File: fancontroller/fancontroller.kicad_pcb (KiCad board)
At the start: 2 copper layers, 84 x 80 mm, 43 parts, among them J1 Power, J2 Serial Conn, M1 FAN0, M2 FAN0, M3 FAN0, M4 FAN0, M5 FAN0, M6 FAN0, Q1 AO3400A, Q10 AO3401A, Q11 AO3400A, Q12 AO3401A, Q2 AO3401A, Q3 AO3400A, Q4 AO3401A, Q5 AO3400A, Q6 AO3401A, Q7 AO3400A, Q8 AO3401A, Q9 AO3400A, SW1 SW_Push, U2 ESP32-WROOM-32, U3 AMS1117-3.3

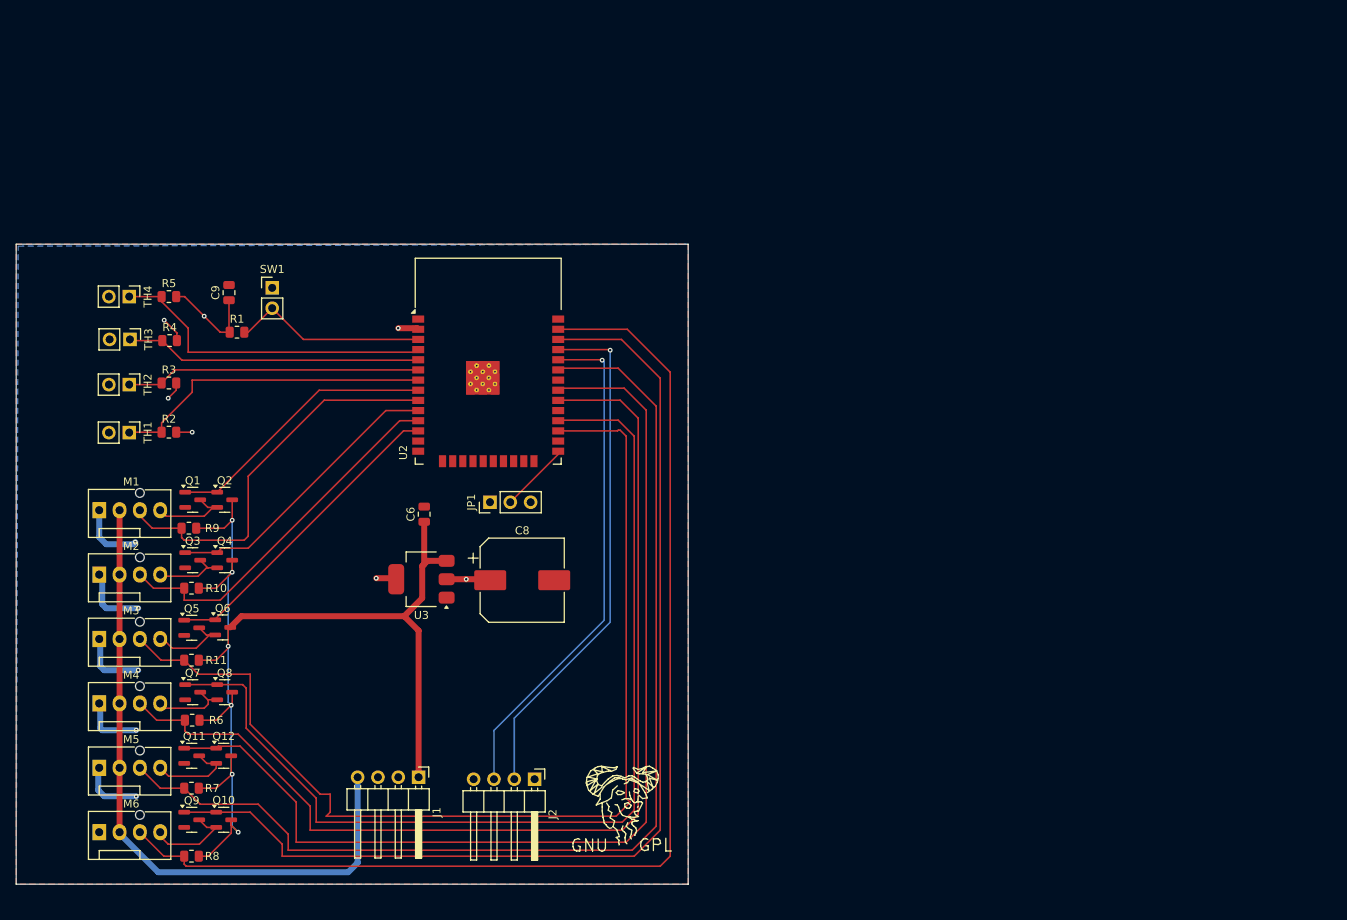
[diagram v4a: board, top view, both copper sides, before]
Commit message: Improve footprints and do massive overhaul for part numbering for better future order
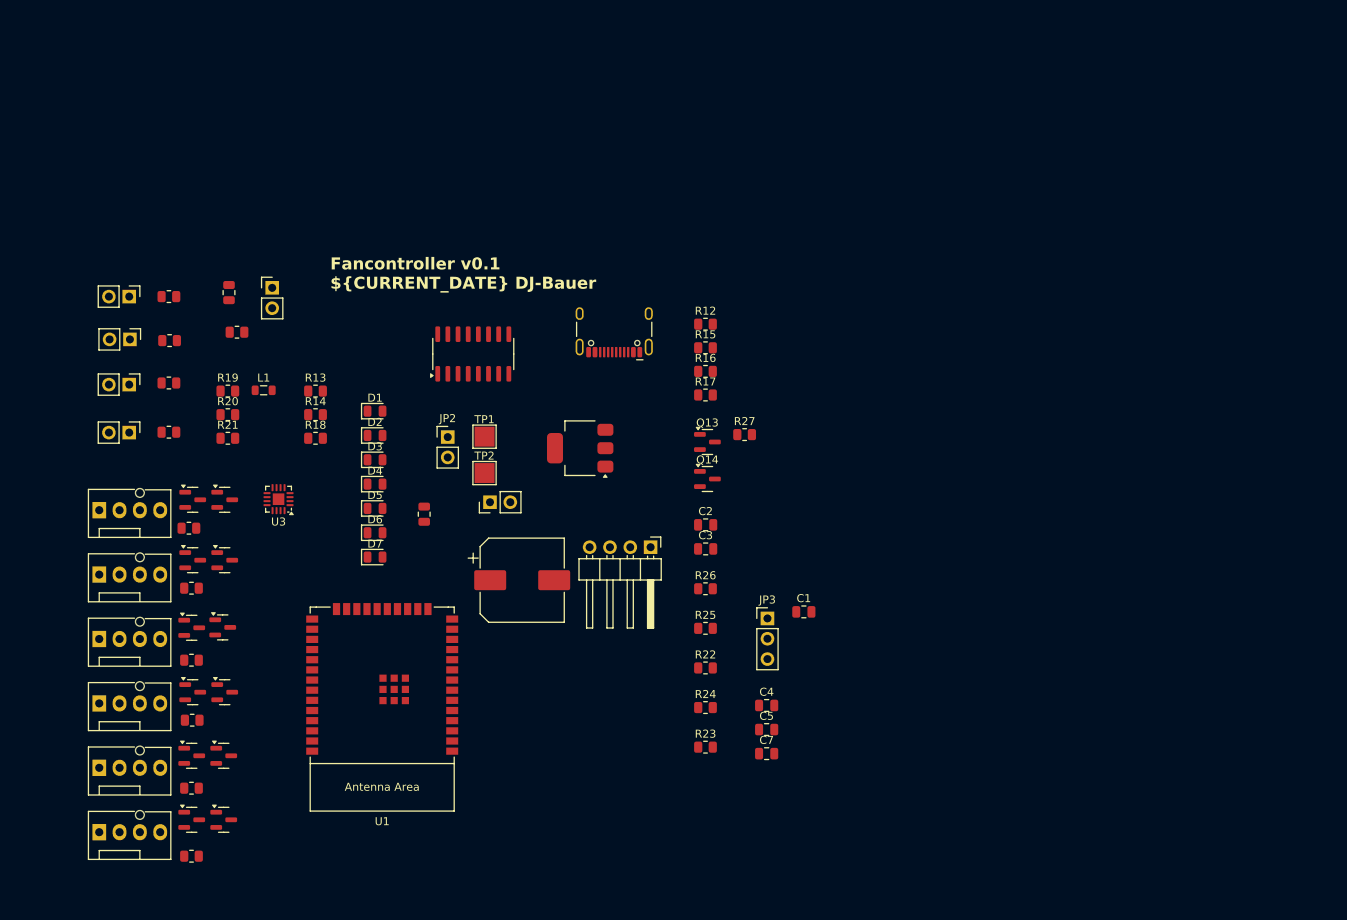
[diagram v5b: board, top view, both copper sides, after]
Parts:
- removed J2: Serial Conn, Connector_PinHeader_2.54mm:PinHeader_1x04_P2.54mm_Horizontal
- removed REF**: Symbol_GNU-Logo_SilkscreenTop, Symbol:Symbol_GNU-Logo_SilkscreenTop
- added C1: 100nF, Capacitor_SMD:C_0805_2012Metric, F.Cu at (122.0, 134.5)
- added C2: 100nF, Capacitor_SMD:C_0805_2012Metric, F.Cu at (109.7, 123.6)
- added C3: 100nF, Capacitor_SMD:C_0805_2012Metric, F.Cu at (109.7, 126.6)
- added C4: 10uF, Capacitor_SMD:C_0805_2012Metric, F.Cu at (117.3, 146.2)
- added C5: 100nF, Capacitor_SMD:C_0805_2012Metric, F.Cu at (117.3, 149.2)
- added C7: 10uF, Capacitor_SMD:C_0805_2012Metric, F.Cu at (117.3, 152.2)
- added D1: EN, LED_SMD:LED_0805_2012Metric, F.Cu at (68.4, 109.4)
- added D2: 3.3V, LED_SMD:LED_0805_2012Metric, F.Cu at (68.4, 112.4)
- added D3: 5V, LED_SMD:LED_0805_2012Metric, F.Cu at (68.4, 115.5)
- added D4: 12V, LED_SMD:LED_0805_2012Metric, F.Cu at (68.4, 118.5)
- added D5: TX, LED_SMD:LED_0805_2012Metric, F.Cu at (68.4, 121.5)
- added D6: RX, LED_SMD:LED_0805_2012Metric, F.Cu at (68.4, 124.6)
- added D7: Reset, LED_SMD:LED_0805_2012Metric, F.Cu at (68.4, 127.6)
- added JP2: PDG is ground, Connector_PinHeader_2.54mm:PinHeader_1x02_P2.54mm_Vertical, F.Cu at (77.4, 112.6)
- added JP3: BOOT, Connector_PinHeader_2.54mm:PinHeader_1x03_P2.54mm_Vertical, F.Cu at (117.4, 135.3)
- added L1: 2.2uH, Inductor_SMD:L_0805_2012Metric, F.Cu at (54.4, 106.8)
- added P2: USB_C_Plug_USB2.0, Connector_USB:USB_C_Receptacle_HCTL_HC-TYPE-C-16P-01A, F.Cu at (98.2, 98.2)
- added Q13: AO3400A, Package_TO_SOT_SMD:SOT-23, F.Cu at (109.9, 113.2)
- added Q14: AO3401A, Package_TO_SOT_SMD:SOT-23, F.Cu at (109.9, 117.8)
- added R12: 60, Resistor_SMD:R_0805_2012Metric, F.Cu at (109.7, 98.5)
- added R13: 65, Resistor_SMD:R_0805_2012Metric, F.Cu at (60.9, 106.9)
- added R14: 150, Resistor_SMD:R_0805_2012Metric, F.Cu at (60.9, 109.8)
- added R15: 1k, Resistor_SMD:R_0805_2012Metric, F.Cu at (109.7, 101.5)
- added R16: 60, Resistor_SMD:R_0805_2012Metric, F.Cu at (109.7, 104.4)
- added R17: 60, Resistor_SMD:R_0805_2012Metric, F.Cu at (109.7, 107.3)
- added R18: 65, Resistor_SMD:R_0805_2012Metric, F.Cu at (60.9, 112.8)
- added R19: 100k, Resistor_SMD:R_0805_2012Metric, F.Cu at (50.0, 106.9)
- added R20: 270k, Resistor_SMD:R_0805_2012Metric, F.Cu at (50.0, 109.8)
- added R21: 51k, Resistor_SMD:R_0805_2012Metric, F.Cu at (50.0, 112.8)
- added R22: 10k, Resistor_SMD:R_0805_2012Metric, F.Cu at (109.7, 141.5)
- added R23: 10k, Resistor_SMD:R_0805_2012Metric, F.Cu at (109.7, 151.4)
- added R24: 10k, Resistor_SMD:R_0805_2012Metric, F.Cu at (109.7, 146.4)
- added R25: 10k, Resistor_SMD:R_0805_2012Metric, F.Cu at (109.7, 136.5)
- added R26: 10k, Resistor_SMD:R_0805_2012Metric, F.Cu at (109.7, 131.6)
- added R27: 10k, Resistor_SMD:R_0805_2012Metric, F.Cu at (114.6, 112.3)
- added TP1: V_out, TestPoint:TestPoint_Pad_2.5x2.5mm, F.Cu at (82.0, 112.6)
- added TP2: PGD, TestPoint:TestPoint_Pad_2.5x2.5mm, F.Cu at (82.0, 117.1)
- added U1: ESP32-WROOM-32, PCM_Espressif:ESP32-WROOM-32E, F.Cu at (69.2, 144.9)
- added U4: AMS1117-3.3, Package_TO_SOT_SMD:SOT-223-3_TabPin2, F.Cu at (94.0, 114.0)
- C6: value 10uF -> 47u
- C9: value 0.1uF -> 100nF
- JP1: value BOOT -> Enable 12V Power; footprint Connector_PinHeader_2.54mm:PinHeader_1x03_P2.54mm_Vertical -> Connector_PinHeader_2.54mm:PinHeader_1x02_P2.54mm_Vertical
- Q1: value AO3400A -> SS8050-G
- Q2: value AO3401A -> SS8050-G
- R10, R11: value 10k -> 470
- R6, R7: value 10k -> 5.1k
- SW1: value SW_Push -> Reset
- TH1: value Thermistor -> Temp0
- TH2: value Thermistor -> Temp1
- TH3: value Thermistor -> Temp2
- TH4: value Thermistor -> Temp3
- U2: value ESP32-WROOM-32 -> CH340C; footprint RF_Module:ESP32-WROOM-32 -> Package_SO:SOIC-16_3.9x9.9mm_P1.27mm
- U3: value AMS1117-3.3 -> BD9D300MUV; footprint Package_TO_SOT_SMD:SOT-223-3_TabPin2 -> Package_DFN_QFN:VQFN-16-1EP_3x3mm_P0.5mm_EP1.45x1.45mm
- moved J1 40.8 mm to (102.8, 126.4)
- moved U3 20.5 mm to (56.3, 120.4)
- moved U2 4.31 mm to (80.6, 102.2), turned to 90 degrees
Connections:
- JP1 pad 1: +3.3V -> +12V
- JP1 pad 2: Net-(JP1-C) -> /Power Delivery/EN
- M1 pad 3: Tacho0 -> /Tacho 1
- M2 pad 3: Tacho1 -> /Tacho 0
- M3 pad 3: Tacho2 -> /Tacho 2
- M4 pad 3: Tacho3 -> /Tacho 3
- M5 pad 3: Tacho4 -> /Tacho 4
- M6 pad 3: Tacho5 -> /Tacho 5
- Q1 pad 1: PWM0 -> Net-(Q1-B)
- Q1 pad 2: GND -> /USB-C Port/RTS
- Q1 pad 3: Net-(M1-PWM) -> EN
- Q10 pad 1: PWM5 -> /PWM 3
- Q10 pad 2: Net-(M6-PWM) -> Net-(M4-PWM)
- Q11 pad 1: PWM4 -> /PWM 4
- Q12 pad 1: PWM4 -> /PWM 4
- Q2 pad 1: PWM0 -> Net-(Q2-B)
- Q2 pad 2: Net-(M1-PWM) -> /USB-C Port/DTR
- Q2 pad 3: +5V -> RST
- Q3 pad 1: PWM1 -> /PWM 1
- Q3 pad 3: Net-(M2-PWM) -> Net-(M1-PWM)
- Q4 pad 1: PWM1 -> /PWM 1
- Q4 pad 2: Net-(M2-PWM) -> Net-(M1-PWM)
- Q5 pad 1: PWM2 -> /PWM 0
- Q5 pad 3: Net-(M3-PWM) -> Net-(M2-PWM)
- Q6 pad 1: PWM2 -> /PWM 0
- Q6 pad 2: Net-(M3-PWM) -> Net-(M2-PWM)
- Q7 pad 1: PWM3 -> /PWM 2
- Q7 pad 3: Net-(M4-PWM) -> Net-(M3-PWM)
- Q8 pad 1: PWM3 -> /PWM 2
- Q8 pad 2: Net-(M4-PWM) -> Net-(M3-PWM)
- Q9 pad 1: PWM5 -> /PWM 3
- Q9 pad 3: Net-(M6-PWM) -> Net-(M4-PWM)
- R1 pad 2: Net-(U2-EN) -> EN
- R10 pad 1: +5V -> Net-(U2-TXD)
- R10 pad 2: Tacho1 -> RX
- R11 pad 1: +5V -> TX
- R11 pad 2: Tacho2 -> Net-(U2-RXD)
- R6 pad 1: +5V -> GND
- R6 pad 2: Tacho3 -> Net-(P2-CC)
- R7 pad 1: +5V -> Net-(P2-VCONN)
- R7 pad 2: Tacho4 -> GND
- R8 pad 1: +5V -> /USB-C Port/DTR
- R8 pad 2: Tacho5 -> Net-(Q1-B)
- R9 pad 1: +5V -> /USB-C Port/RTS
- R9 pad 2: Tacho0 -> Net-(Q2-B)
- SW1 pad 2: Net-(U2-EN) -> EN
- U2 pad 10: PWM1 -> unconnected-(U2-~{DSR}-Pad10)
- U2 pad 11: Tacho1 -> unconnected-(U2-~{RI}-Pad11)
- U2 pad 12: PWM2 -> unconnected-(U2-~{DCD}-Pad12)
- U2 pad 13: unconnected-(U2-IO14-Pad13) -> /USB-C Port/DTR
- U2 pad 14: unconnected-(U2-IO12-Pad14) -> /USB-C Port/RTS
- U2 pad 16: unconnected-(U2-IO13-Pad16) -> +3.3V
- U2 pad 2: +3.3V -> Net-(U2-TXD)
- U2 pad 3: Net-(U2-EN) -> Net-(U2-RXD)
- U2 pad 4: TMP3 -> Net-(U2-V3)
- U2 pad 5: TMP2 -> Net-(P2-D+)
- U2 pad 6: TMP1 -> Net-(P2-D-)
- U2 pad 7: TMP0 -> unconnected-(U2-NC-Pad7)
- U2 pad 8: PWM0 -> unconnected-(U2-NC-Pad8)
- U2 pad 9: Tacho0 -> unconnected-(U2-~{CTS}-Pad9)
- U3 pad 1: GND -> Net-(L1-Pad1)
- U3 pad 2: +3.3V -> Net-(L1-Pad1)
- U3 pad 3: +5V -> Net-(L1-Pad1)
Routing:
- net Tacho5: track 145.9 -> 0.00 mm
- net +5V: track 142.5 -> 0.00 mm, vias 6 -> 0
- net Tacho4: track 138.0 -> 0.00 mm
- net PWM5: track 135.3 -> 0.00 mm
- net Tacho3: track 132.7 -> 0.00 mm
- net Tacho2: track 132.0 -> 0.00 mm
- net PWM4: track 130.5 -> 0.00 mm
- net PWM3: track 125.7 -> 0.00 mm
- net +12V: track 83.4 -> 0.00 mm
- net TX: track 65.1 -> 0.00 mm, vias 1 -> 0
- net RX: track 63.7 -> 0.00 mm, vias 1 -> 0
- net Tacho0: track 49.1 -> 0.00 mm
- net Tacho1: track 46.3 -> 0.00 mm
- net TMP3: track 41.3 -> 0.00 mm
- net GND: track 41.0 -> 0.00 mm, vias 5 -> 0
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- removed copper zone on B.Cu, net +3.3V
- removed copper zone on F.Cu, net GND
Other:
- board outline removed
- board text added: "${TITLE} ${REVISION} ${CURRENT_DATE} ${COMPANY}"

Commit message: Pretty rounded edgecut around pcb and start laying out LEDs
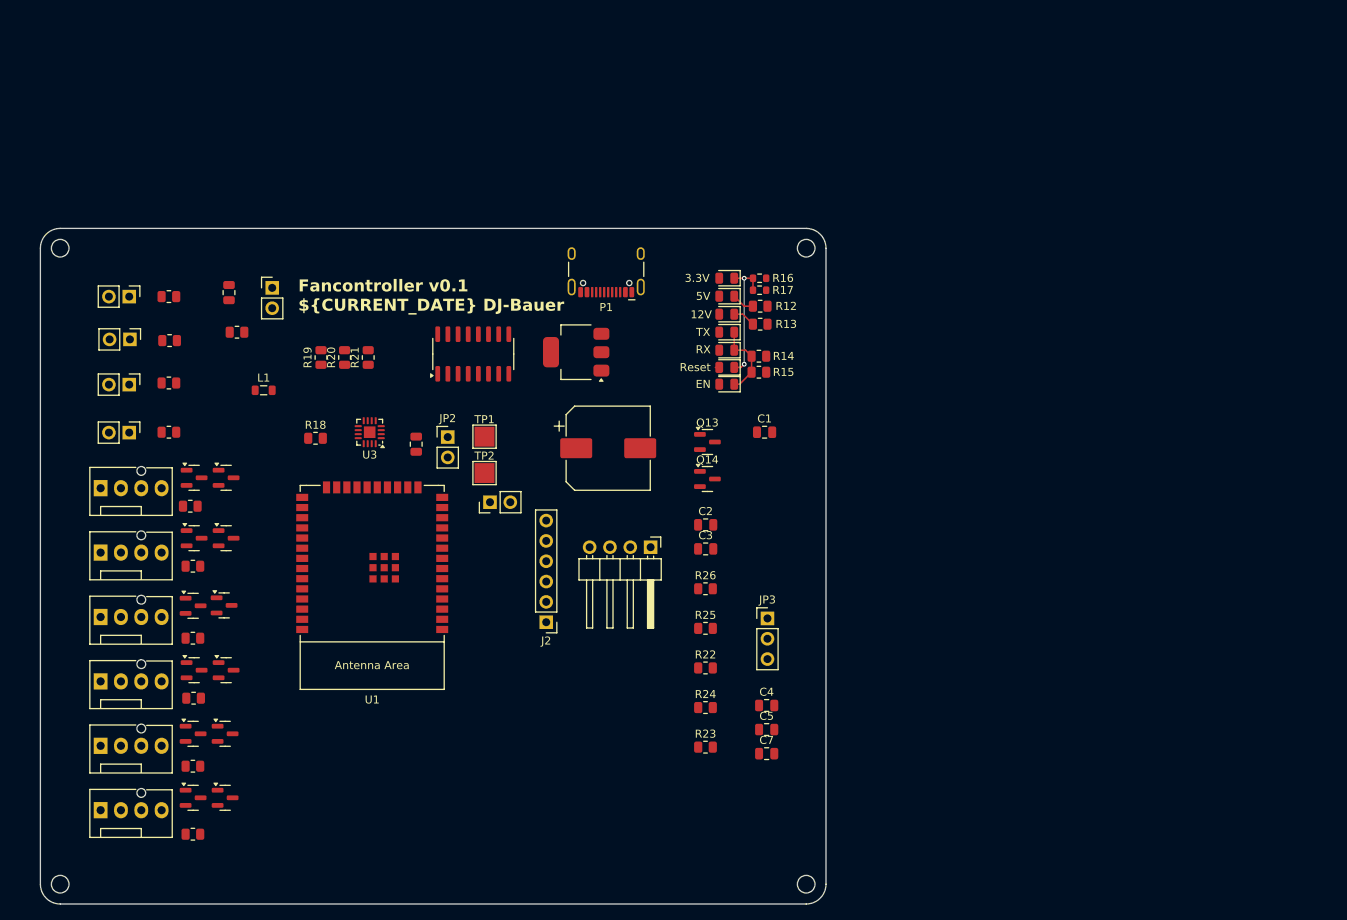
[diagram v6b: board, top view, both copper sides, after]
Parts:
- removed P2: USB_C_Plug_USB2.0, Connector_USB:USB_C_Receptacle_HCTL_HC-TYPE-C-16P-01A
- removed R27: 10k, Resistor_SMD:R_0805_2012Metric
- added H1: MountingHole_2.2mm_M2, MountingHole:MountingHole_2.2mm_M2, F.Cu at (122.2, 89.0)
- added H2: MountingHole_2.2mm_M2, MountingHole:MountingHole_2.2mm_M2, F.Cu at (122.2, 168.5)
- added H3: MountingHole_2.2mm_M2, MountingHole:MountingHole_2.2mm_M2, F.Cu at (29.0, 168.5)
- added H4: MountingHole_2.2mm_M2, MountingHole:MountingHole_2.2mm_M2, F.Cu at (29.0, 89.0)
- added J2: Debug, Connector_PinHeader_2.54mm:PinHeader_1x06_P2.54mm_Vertical, F.Cu at (89.8, 135.8)
- added P1: USB_C_Plug_USB2.0, Connector_USB:USB_C_Receptacle_HCTL_HC-TYPE-C-16P-01A, F.Cu at (97.2, 90.8)
- 12V: renamed from D2; value 3.3V -> 12V
- 3.3V: renamed from D6; value RX -> 3.3V
- 5V: renamed from D1; value EN -> 5V
- EN: renamed from D4; value 12V -> EN
- R12: value 60 -> 150
- R13: value 65 -> 1k
- R14: value 150 -> 120
- R15: value 1k -> 120
- R16: value 60 -> 220; footprint Resistor_SMD:R_0805_2012Metric -> Resistor_SMD:R_0603_1608Metric
- R17: value 60 -> 100; footprint Resistor_SMD:R_0805_2012Metric -> Resistor_SMD:R_0603_1608Metric
- R18: value 65 -> 100k
- R19: value 100k -> 270k
- R20: value 270k -> 51k
- R21: value 51k -> 10k
- RX: renamed from D5; value TX -> RX
- TX: renamed from D3; value 5V -> TX
- moved R13 56.2 mm to (116.5, 98.5), turned to 180 degrees
- moved R14 55.9 mm to (116.3, 102.5), turned to 180 degrees
- moved 3.3V 54.3 mm to (112.3, 92.8), turned to 180 degrees
- moved Reset 49.9 mm to (112.3, 103.9), turned to 180 degrees
- moved RX 48.2 mm to (112.3, 101.8), turned to 180 degrees
- moved TX 46.8 mm to (112.3, 99.5), turned to 180 degrees
- moved 12V 46.5 mm to (112.3, 97.2), turned to 180 degrees
- moved 5V 46.2 mm to (112.3, 95.0), turned to 180 degrees
- moved EN 45.7 mm to (112.3, 106.0), turned to 180 degrees
- moved C1 23.0 mm to (117.0, 112.0)
- moved R21 20.2 mm to (67.5, 102.7), turned to 90 degrees
- moved C8 19.7 mm to (97.5, 114.0)
- moved R20 16.3 mm to (64.5, 102.7), turned to 90 degrees
- moved U1 15.3 mm to (68.0, 129.7)
- moved R17 14.7 mm to (116.4, 94.2), turned to 180 degrees
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- renumbered D7 to Reset
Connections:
- net /USB-C Port/DTR renamed DTR
- net /USB-C Port/RTS renamed RTS
- 12V pad 2: +3.3V -> +12V
- 3.3V pad 2: RX -> +3.3V
- 5V pad 2: EN -> +5V
- EN pad 1: Net-(D4-K) -> Net-(D3-K)
- EN pad 2: +12V -> EN
- R15 pad 2: Net-(D4-K) -> Net-(D3-K)
- R16 pad 2: Net-(D5-K) -> Net-(D6-K)
- R18 pad 1: GND -> /Power Delivery/PGD
- R18 pad 2: Net-(D7-K) -> +5V
- R19 pad 1: /Power Delivery/PGD -> +5V
- R19 pad 2: +5V -> Net-(U3-FB)
- R20 pad 1: +5V -> Net-(U3-FB)
- R20 pad 2: Net-(U3-FB) -> GND
- R21 pad 1: Net-(U3-FB) -> +3.3V
- R21 pad 2: GND -> /Tacho 1
- R22 pad 2: /Tacho 1 -> /Tacho 0
- R23 pad 2: /Tacho 0 -> /Tacho 2
- R24 pad 2: /Tacho 2 -> /Tacho 3
- R25 pad 2: /Tacho 3 -> /Tacho 4
- R26 pad 2: /Tacho 4 -> /Tacho 5
- RX pad 1: Net-(D5-K) -> Net-(D3-K)
- RX pad 2: TX -> RX
- Reset pad 1: Net-(D7-K) -> Net-(D6-K)
- TX pad 2: +5V -> TX
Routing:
- net Net-(D6-K): track 0.00 -> 16.0 mm, vias 0 -> 2
- net Net-(D3-K): track 0.00 -> 9.53 mm
- net Net-(D2-K): track 0.00 -> 2.86 mm
- net Net-(D1-K): track 0.00 -> 2.86 mm
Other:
- board outline added: 98.2 x 84.4 mm

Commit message: Begin placing parts for v0.1 layout
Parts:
- J1: footprint Connector_PinHeader_2.54mm:PinHeader_1x04_P2.54mm_Horizontal -> Connector_PinHeader_2.54mm:PinHeader_1x04_P2.54mm_Vertical
- moved Q13 78.4 mm to (45.6, 158.0)
- moved Q14 72.5 mm to (49.6, 158.0)
- moved R26 70.7 mm to (45.6, 161.5)
- moved L1 67.7 mm to (103.4, 153.5)
- moved R22 67.6 mm to (45.4, 120.5)
- moved R25 66.2 mm to (45.6, 153.0)
- moved R23 65.7 mm to (45.6, 137.0)
- moved R24 64.1 mm to (45.6, 145.0)
- moved U3 54.1 mm to (96.6, 157.8), turned to -90 degrees
- moved R11 52.8 mm to (84.9, 102.5), turned to 0 degrees
- moved C8 49.0 mm to (109.5, 161.5)
- moved U4 48.6 mm to (86.0, 150.0)
- moved R10 48.6 mm to (85.1, 100.5)
- moved TP1 41.1 mm to (99.0, 150.0)
- moved J1 40.3 mm to (99.0, 166.5)
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- renumbered 5V to D1, 12V to D2, TX to D3, EN to D4, RX to D5, 3.3V to D6, Reset to D7
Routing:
- net +12V: track 0.00 -> 10.7 mm
- net +5V: track 0.00 -> 8.68 mm
- net /Power Delivery/PGD: track 0.00 -> 6.65 mm
- added copper zone on F.Cu, net GND

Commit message: edit schematic
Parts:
- U3: footprint Package_DFN_QFN:VQFN-16-1EP_3x3mm_P0.5mm_EP1.45x1.45mm -> DJCustom:VQFN-16-1EP_3x3mm_P0.5mm_EP1.45x1.45mm
- U4: footprint Package_TO_SOT_SMD:SOT-223-3_TabPin2 -> Package_TO_SOT_SMD:SOT-223
- moved M6 83.5 mm to (113.8, 134.4), turned to 90 degrees
- moved R26 80.3 mm to (116.0, 122.9), turned to -90 degrees
- moved C8 78.2 mm to (47.5, 113.8), turned to -90 degrees
- moved Q13 75.6 mm to (112.5, 122.9), turned to 90 degrees
- moved Q14 74.1 mm to (112.5, 118.9), turned to 90 degrees
- moved M5 73.6 mm to (105.7, 134.4), turned to 90 degrees
- moved C7 71.2 mm to (48.0, 135.5), turned to 180 degrees
- moved J1 70.8 mm to (37.5, 131.5), turned to 180 degrees
- moved R25 68.8 mm to (107.5, 122.9), turned to -90 degrees
- moved Q11 64.4 mm to (104.2, 122.9), turned to 90 degrees
- moved M4 64.2 mm to (97.7, 134.4), turned to 90 degrees
- moved Q12 62.7 mm to (104.2, 118.9), turned to 90 degrees
- moved C5 62.2 mm to (43.0, 128.4), turned to 90 degrees
- moved C4 61.0 mm to (42.0, 124.0), turned to 90 degrees
- moved C1 58.6 mm to (60.0, 98.5), turned to 180 degrees
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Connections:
- U1 pad 11: /Tacho 1 -> /Tacho 0
- U1 pad 12: /PWM 2 -> /PWM 0
- U1 pad 27: /Tacho 2 -> /PWM 5
- U1 pad 28: /PWM 3 -> /Tacho 5
- U1 pad 36: /PWM 5 -> /PWM 3
- U1 pad 37: /Tacho 5 -> /Tacho 2
- U1 pad 8: /PWM 0 -> /PWM 2
- U1 pad 9: /Tacho 0 -> /Tacho 1
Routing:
- net +5V: track 8.68 -> 154.3 mm, vias 0 -> 3
- net +12V: track 10.7 -> 134.6 mm, vias 0 -> 1
- net EN: track 0.00 -> 66.8 mm, vias 0 -> 2
- net /Tacho 2: track 0.00 -> 51.3 mm, vias 0 -> 2
- net GND: track 0.43 -> 51.5 mm
- net RST: track 0.00 -> 49.2 mm, vias 0 -> 1
- net /PWM 3: track 0.00 -> 47.5 mm, vias 0 -> 2
- net +3.3V: track 0.00 -> 47.3 mm, vias 0 -> 14
- net TX: track 0.00 -> 47.1 mm, vias 0 -> 3
- net RX: track 0.00 -> 45.1 mm, vias 0 -> 3
- net /Tacho 1: track 0.00 -> 37.9 mm, vias 0 -> 2
- net /Tacho 0: track 0.00 -> 36.4 mm, vias 0 -> 2
- net /PWM 2: track 0.00 -> 34.4 mm, vias 0 -> 2
- net TMP3: track 0.00 -> 31.3 mm
- net TMP0: track 0.00 -> 30.7 mm
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- added copper zone on B.Cu, net +3.3V
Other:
- board size 98.2 x 84.4 mm -> 96.2 x 53.4 mm
